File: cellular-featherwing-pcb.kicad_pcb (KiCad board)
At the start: 2 copper layers, 54 x 27 mm, 108 parts, among them J1 SIM8060-6-0-14-00-A, J2 TSM-116-01-L-SV, J3 TSM-112-01-L-SV, J4 U.FL-R-SMT, J5 U.FL-R-SMT, U1 BG96, U2 TPS63020QDSJTQ1, U3 TXB0108DQSR, U4 MAX8868EUK30+T

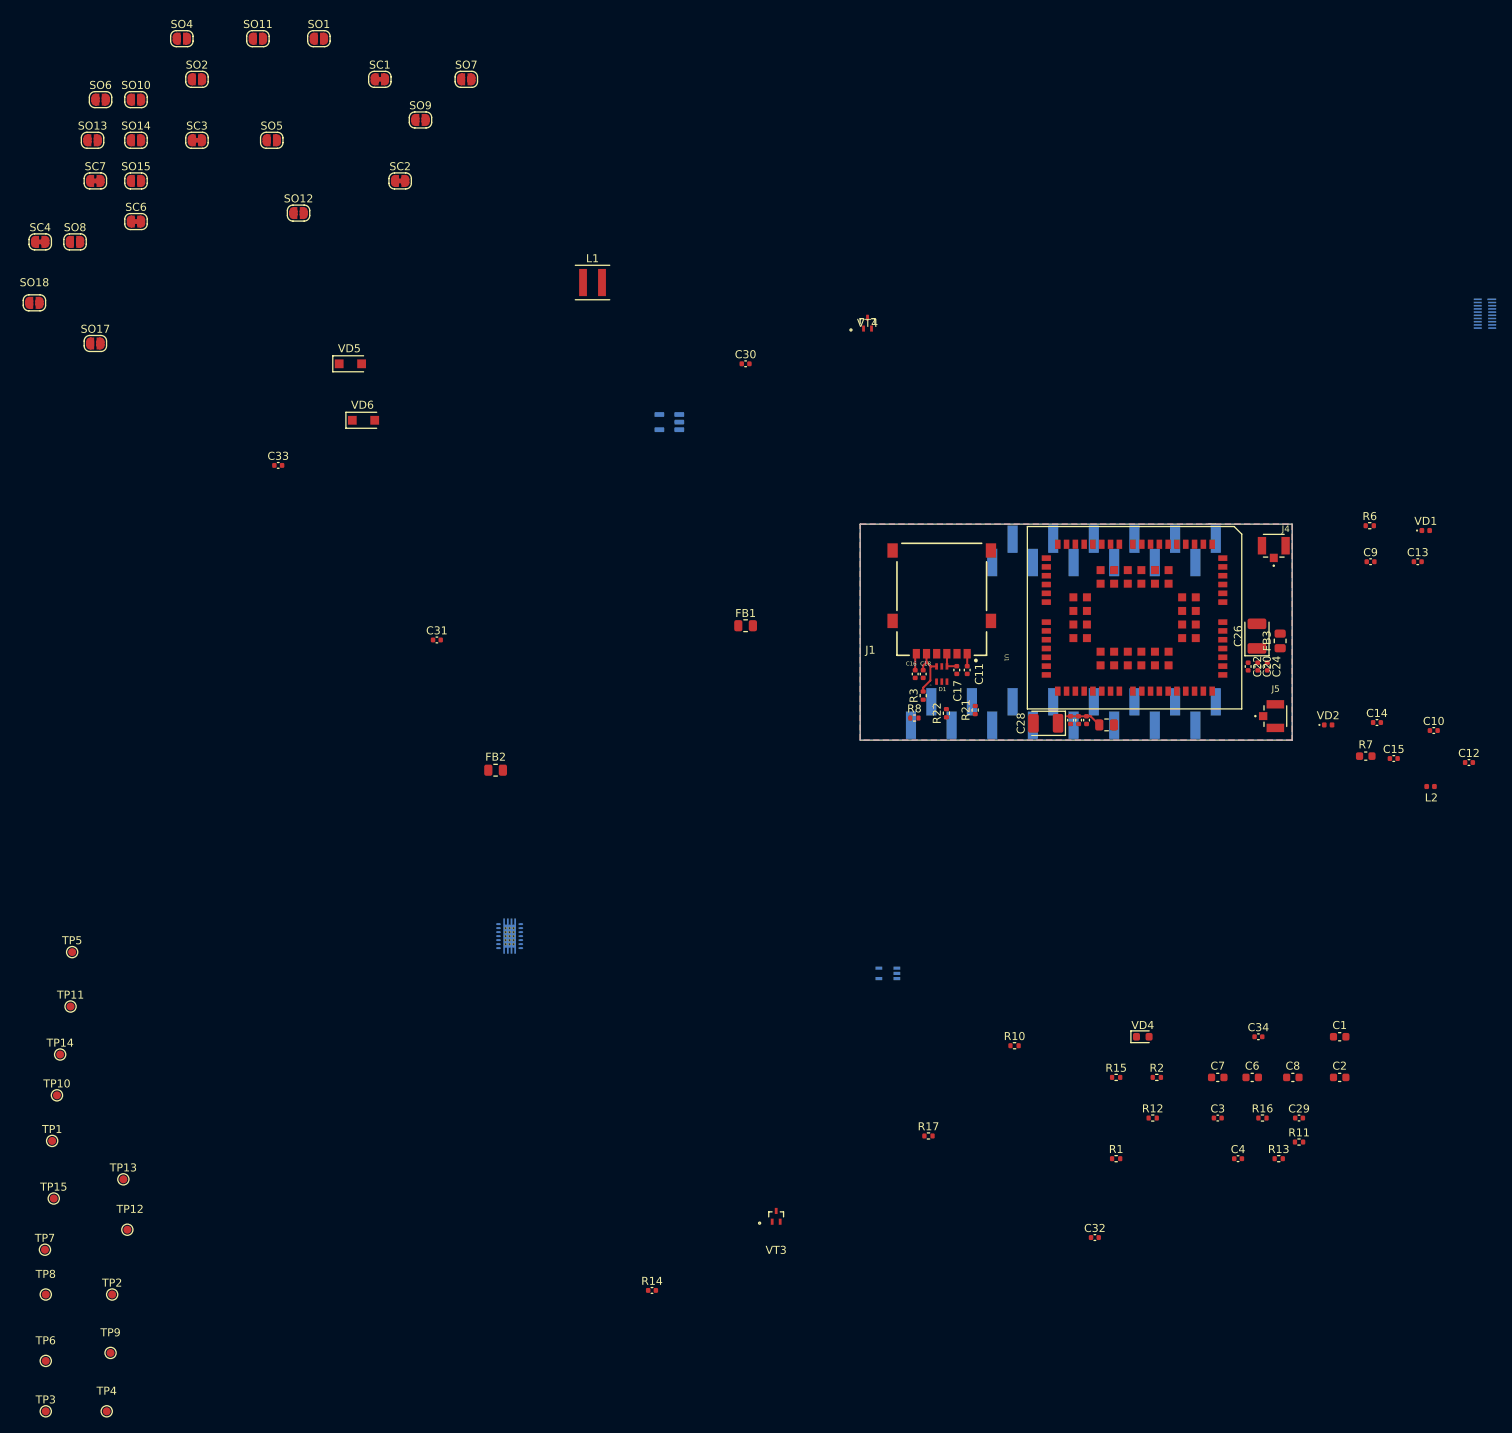
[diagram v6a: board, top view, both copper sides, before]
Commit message: Placed all components
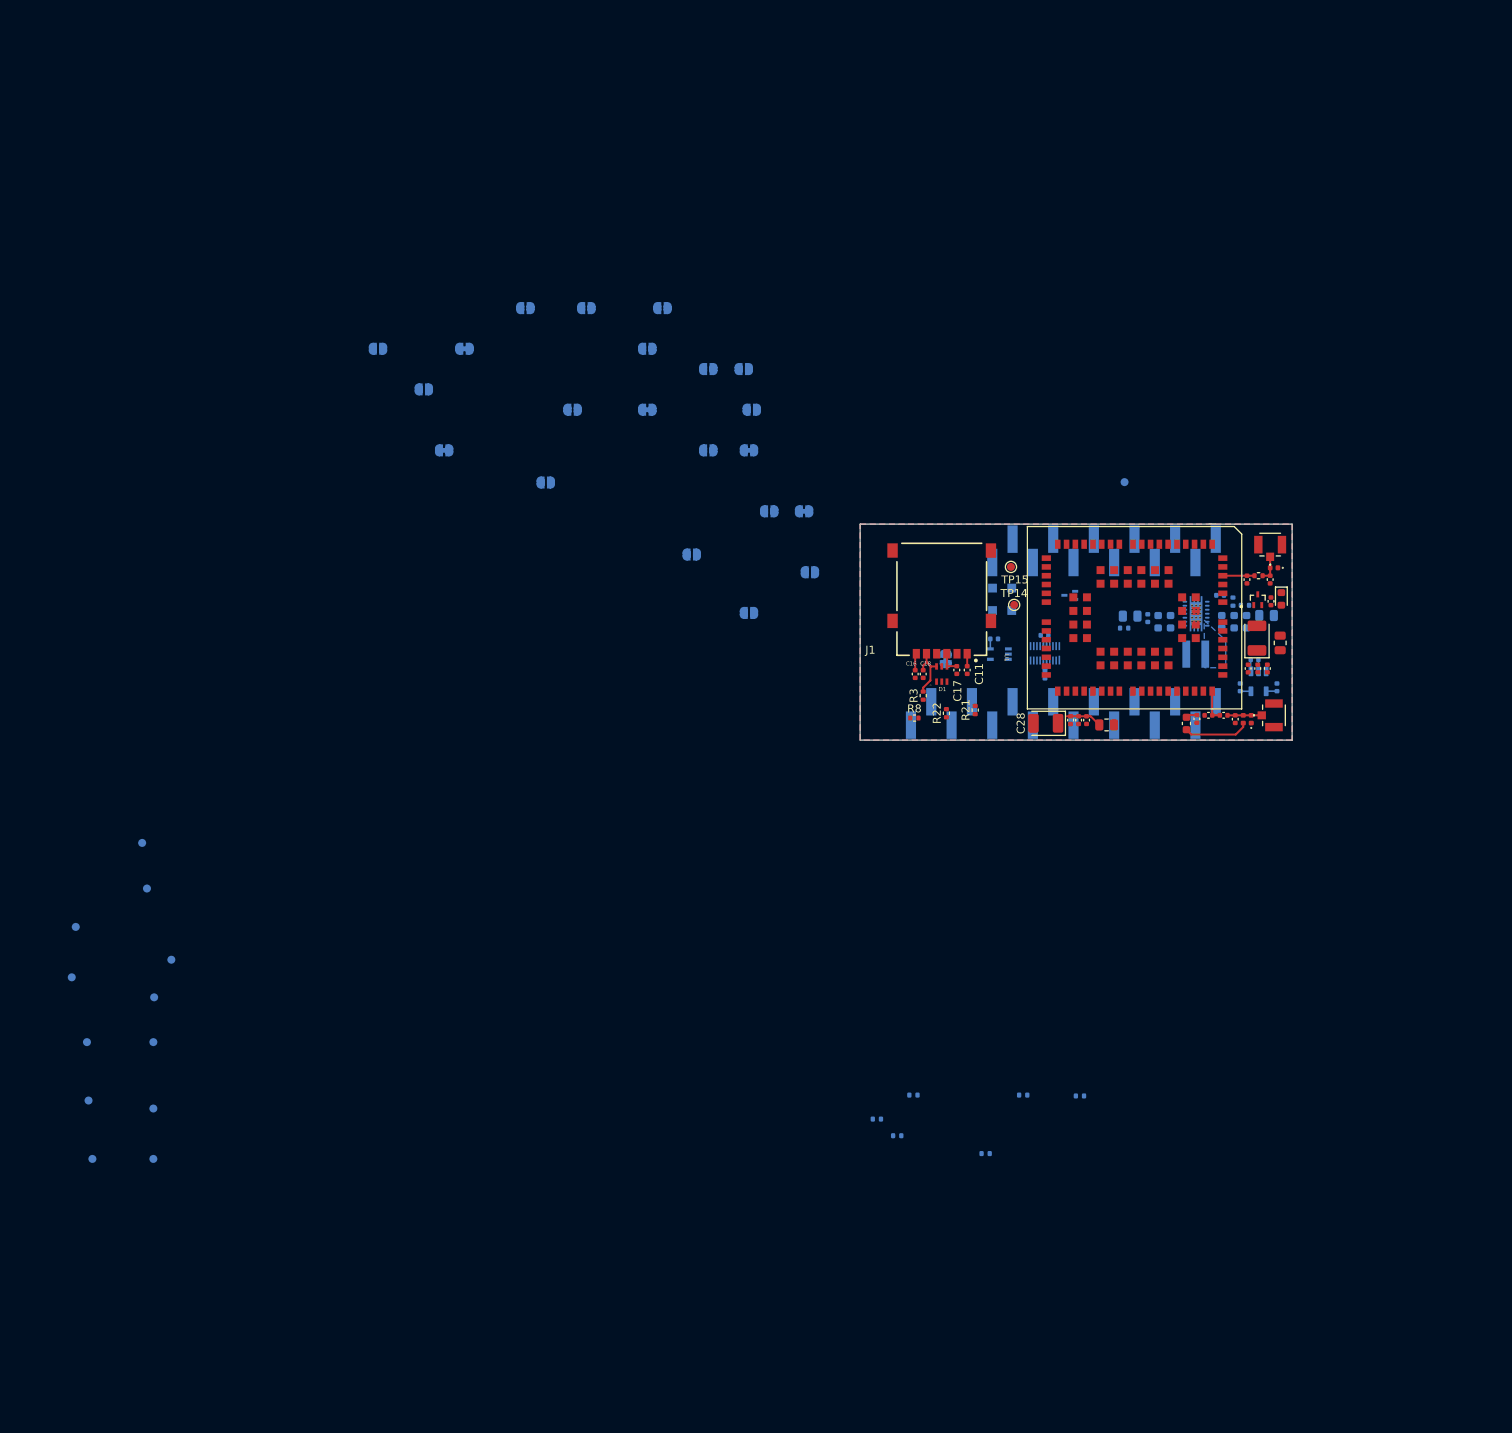
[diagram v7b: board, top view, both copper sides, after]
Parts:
- C1, C2, C29, C3, C30, C31, C32, C33, C34, C4, C6, C7, C8, FB1, FB2, L1, R1, R10, R11, R12, R13, R15, R16, R17, R2, SC1, SC2, SC3, SC4, SC6, SC7, SO1, SO10, SO11, SO12, SO13, SO14, SO15, SO17, SO18, SO2, SO4, SO5, SO6, SO7, SO8, SO9, TP1, TP10, TP11, TP12, TP13, TP2, TP3, TP4, TP5, TP6, TP7, TP8, TP9, VD5, VD6, VT4: moved to B.Cu
- moved TP11 147.2 mm to (154.1, 75.8), turned to 180 degrees
- moved TP15 143.4 mm to (139.8, 86.3)
- moved TP14 131.8 mm to (140.2, 91.1)
- moved C33 123.4 mm to (168.5, 101.4), turned to 90 degrees
- moved R14 115.8 mm to (172.3, 90.7), turned to -90 degrees
- moved SC6 115.0 mm to (131.7, 97.8), turned to -90 degrees
- moved C31 105.2 mm to (173.1, 101.4), turned to 90 degrees
- moved SO18 102.6 mm to (114.7, 87.0), turned to 180 degrees
- moved SC4 101.2 mm to (114.0, 79.4), turned to 180 degrees
- moved FB2 98.3 mm to (171.8, 92.4)
- moved VT3 97.8 mm to (170.7, 90.5)
- moved U2 94.8 mm to (163.0, 92.2)
- moved SO8 93.1 mm to (109.6, 79.4), turned to 180 degrees
- moved SO13 89.0 mm to (107.5, 66.7), turned to 180 degrees
- moved L1 88.6 mm to (162.9, 97.2), turned to 180 degrees
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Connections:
- net Net-(L1-Pad1) renamed /L1_1
- net Net-(L1-Pad2) renamed /L1_2
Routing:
- net Net-(L2-Pad2): track 0.00 -> 8.23 mm
- net Net-(C10-Pad1): track 0.00 -> 4.28 mm
- net 3V3: track 0.00 -> 4.05 mm
- net GPS_ANT: track 0.00 -> 3.97 mm
- net GSM_ANT: track 0.00 -> 3.96 mm
- net Net-(C9-Pad1): track 0.00 -> 3.30 mm
- net GND: track 0.00 -> 2.95 mm
- net VDD_EXT: track 0.00 -> 2.71 mm
- net VMODEM: track 0.00 -> 1.47 mm
- net GPS_ANT_VDD: track 0.00 -> 1.41 mm
- net Net-(C33-Pad1): track 0.00 -> 1.36 mm
- net /L1_2: track 0.00 -> 0.50 mm
- added copper zone on B.Cu, net /L1_1

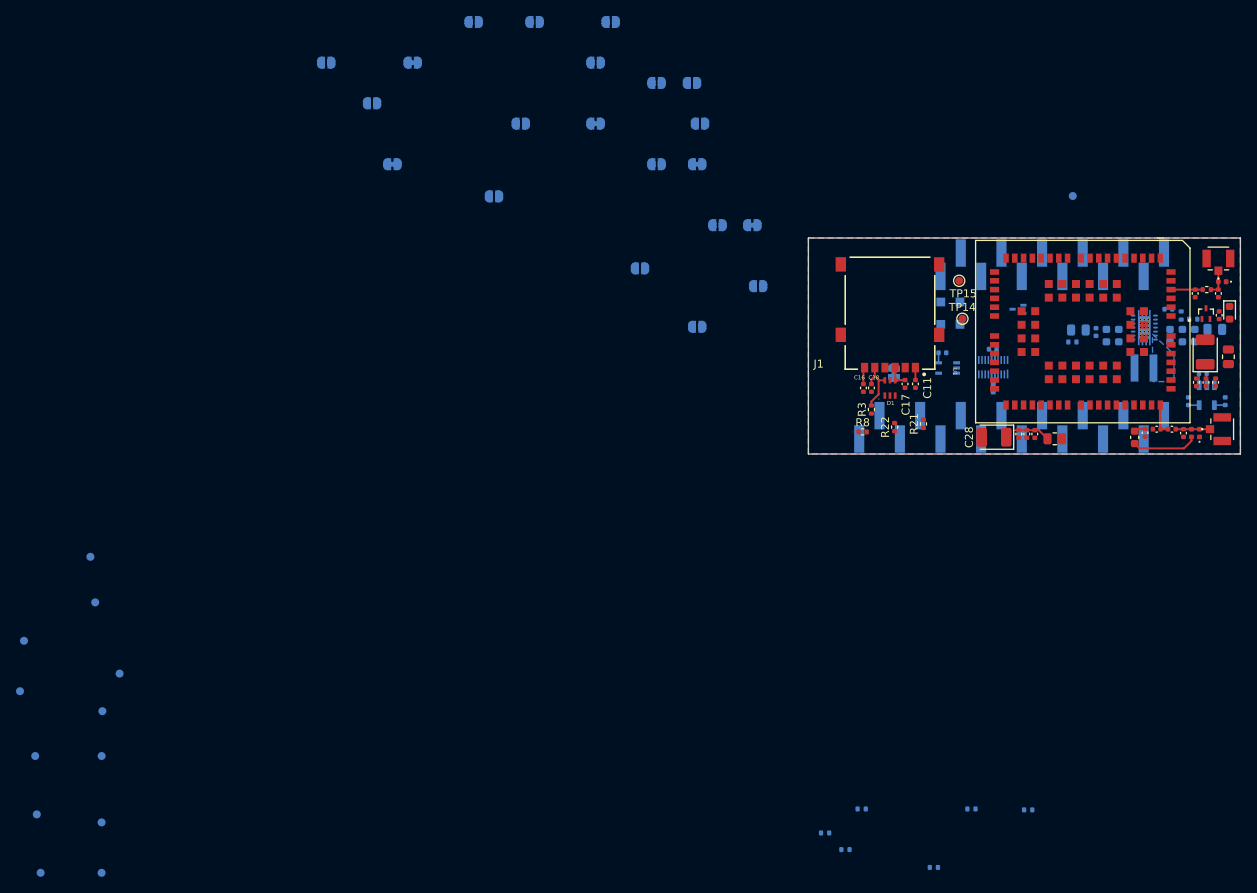
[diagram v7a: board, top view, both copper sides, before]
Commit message: All components placed
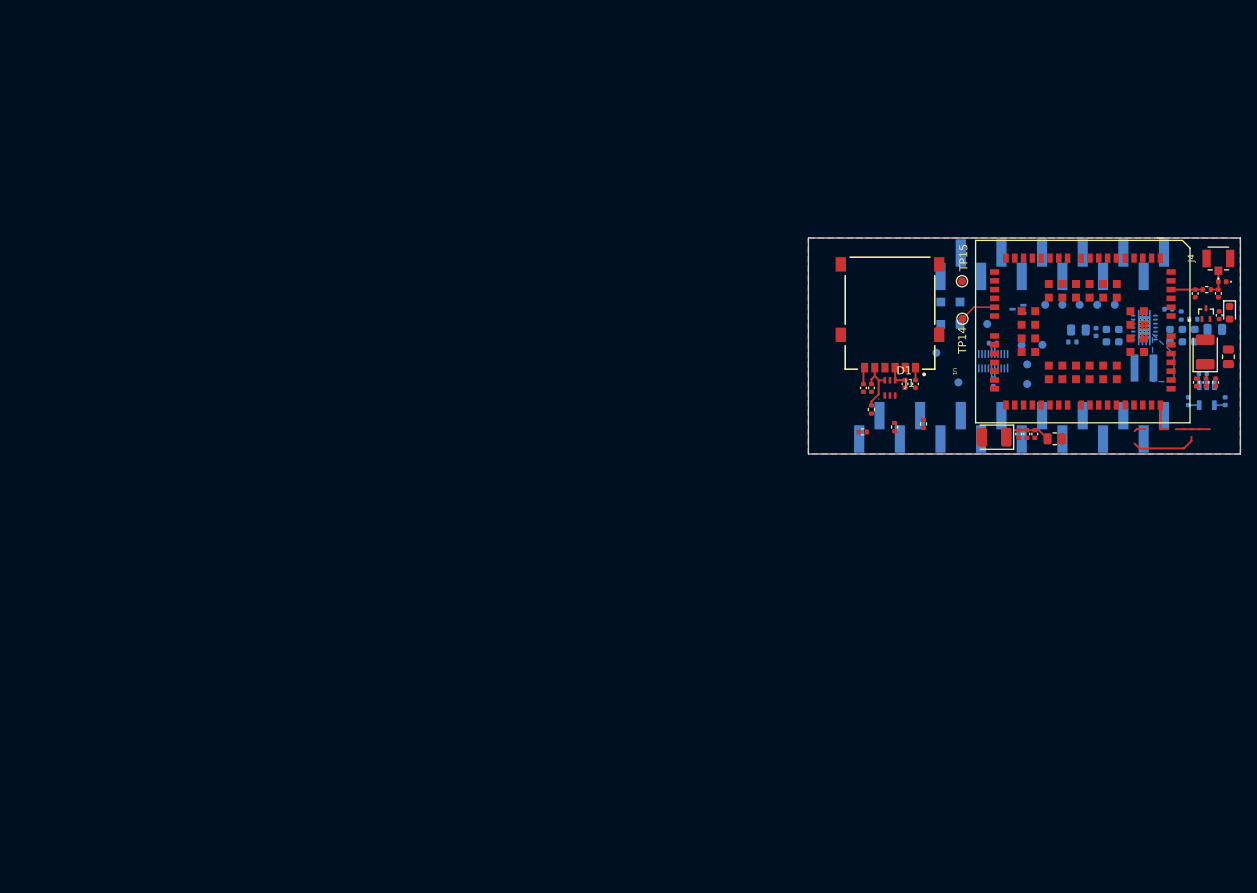
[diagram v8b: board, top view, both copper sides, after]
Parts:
- removed C10, C14: DNP, Capacitor_SMD:C_0402_1005Metric
- removed C12: 100pF, Capacitor_SMD:C_0402_1005Metric
- removed C15: 0.1uF, Capacitor_SMD:C_0402_1005Metric
- removed C32: 0.1, Capacitor_SMD:C_0402_1005Metric
- removed DD1: SN74AHC1G09DCKR, SN74AHC1G09DCKR:SN74AHC1G09DCKR
- removed J5: U.FL-R-SMT, U_fl_conn:HRS_U.FL-R-SMT(10)
- removed L2: 47nH, Inductor_SMD:L_0402_1005Metric
- removed R10, R16, R17: 10k, Resistor_SMD:R_0402_1005Metric
- removed R11, R12, R13: 1k, Resistor_SMD:R_0402_1005Metric
- removed R7: 10, Capacitor_SMD:C_0603_1608Metric
- removed SC1, SC2, SC3, SC4, SC6, SC7: SolderJumper_2_Bridged, Jumper:SolderJumper-2_P1.3mm_Bridged_RoundedPad1.0x1.5mm
- removed SO1, SO10, SO11, SO12, SO13, SO14, SO15, SO17, SO18, SO2, SO4, SO5, SO6, SO7, SO8, SO9: SolderJumper_2_Open, Jumper:SolderJumper-2_P1.3mm_Open_RoundedPad1.0x1.5mm
- removed TP7: TestPoint, TestPoint:TestPoint_Pad_D1.0mm
- removed VD2: D_TVS, Diode_SMD:D_0402_1005Metric
- moved TP9 149.0 mm to (159.3, 89.3)
- moved TP12 139.0 mm to (152.8, 89.3)
- moved TP4 136.8 mm to (143.3, 91.8)
- moved TP2 136.0 mm to (150.2, 94.3)
- moved TP13 134.4 mm to (150.6, 89.3)
- moved TP3 132.6 mm to (147.7, 94.4)
- moved TP10 129.7 mm to (157.1, 89.3)
- moved TP6 128.0 mm to (148.3, 99.2)
- moved TP1 120.2 mm to (148.3, 96.8)
- moved TP8 116.8 mm to (139.8, 99.0)
- moved TP5 109.7 mm to (137.0, 95.3)
- moved TP11 13.6 mm to (154.9, 89.3)
- moved C29 0.75 mm to (144.1, 99.0)
- moved C34 0.75 mm to (144.1, 94.2)
- moved U3 0.75 mm to (144.1, 96.4)
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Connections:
- J2 pad 14: GSM_TXD_ESP32 -> GSM_TXD
- J2 pad 15: GSM_RXD_ESP32 -> GSM_RXD
- U3 pad 3: RTS_GPS_RXD -> RTS
- U3 pad 4: CTS_GPS_TXD -> CTS
- VD4 pad 2: Net-(SC7-Pad1) -> VDD
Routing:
- net (no net): track 0.00 -> 13.9 mm
- net Net-(L2-Pad2): track 8.23 -> 0.00 mm
- net DBG_TXD: track 0.00 -> 4.62 mm
- net Net-(C10-Pad1): track 4.28 -> 0.00 mm
- net GPS_ANT_VDD: track 1.41 -> 0.00 mm
- net 3V3: track 4.05 -> 2.80 mm
